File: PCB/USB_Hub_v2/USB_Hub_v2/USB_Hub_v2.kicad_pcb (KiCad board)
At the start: 2 copper layers, 63.2 x 106.8 mm, 54 parts, among them J1 USB_A, J2 USB_A, J3 USB_A, J4 USB_A, J5 USB_A, J6 USB_A, SW1 SW_Push_DPDT, U1 FE1.1s, U2 TS3USB30EDGSR, U3 TPS2116DRL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

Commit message: Update PCB layout: stackup, nets and footprints
Add recent PCB backup archives and apply extensive KiCad PCB updates: define board stackup and layer types (B.Cu -> power), rename/reorder nets, and replace/update multiple footprints and component properties (resistors, capacitors, pads, models, references and values). Adjust pad positions, sizes and net assignments, update 3D model links and footprint metadata to match revised layout. These changes appear to be automated footprint/housekeeping edits and netlist/stack adjustments to prepare the board for updated fabrication/assembly.
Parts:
- added C14: 22p, Capacitor_SMD:C_0805_2012Metric_Pad1.18x1.45mm_HandSolder, F.Cu at (75.7, 104.8)
- added C15: 22p, Capacitor_SMD:C_0805_2012Metric_Pad1.18x1.45mm_HandSolder, F.Cu at (71.5, 104.8)
- added C16: 2n2, Capacitor_SMD:C_0805_2012Metric_Pad1.18x1.45mm_HandSolder, F.Cu at (30.6, 109.2)
- added C17: 2n2, Capacitor_SMD:C_0805_2012Metric_Pad1.18x1.45mm_HandSolder, F.Cu at (29.6, 90.8)
- added C18: 2n2, Capacitor_SMD:C_0805_2012Metric_Pad1.18x1.45mm_HandSolder, F.Cu at (30.1, 76.5)
- added C19: 2n2, Capacitor_SMD:C_0805_2012Metric_Pad1.18x1.45mm_HandSolder, F.Cu at (30.3, 56.9)
- added C20: 2n2, Capacitor_SMD:C_0805_2012Metric_Pad1.18x1.45mm_HandSolder, F.Cu at (109.1, 126.6)
- added C21: 2n2, Capacitor_SMD:C_0805_2012Metric_Pad1.18x1.45mm_HandSolder, F.Cu at (36.0, 126.2)
- added C22: 100n, Capacitor_SMD:C_0805_2012Metric_Pad1.18x1.45mm_HandSolder, F.Cu at (98.5, 108.1)
- added C23: 10u, Capacitor_SMD:C_0805_2012Metric_Pad1.18x1.45mm_HandSolder, F.Cu at (80.7, 106.3)
- added C24: 100n, Capacitor_SMD:C_0805_2012Metric_Pad1.18x1.45mm_HandSolder, F.Cu at (99.1, 99.5)
- added C25: 10u, Capacitor_SMD:C_0805_2012Metric_Pad1.18x1.45mm_HandSolder, F.Cu at (99.1, 102.6)
- added C26: 4u7, Capacitor_SMD:C_0805_2012Metric_Pad1.18x1.45mm_HandSolder, F.Cu at (59.5, 86.2)
- added C27: 100n, Capacitor_SMD:C_0805_2012Metric_Pad1.18x1.45mm_HandSolder, F.Cu at (57.4, 86.2)
- added C28: 4u7, Capacitor_SMD:C_0805_2012Metric_Pad1.18x1.45mm_HandSolder, F.Cu at (59.2, 103.5)
- added C29: 100n, Capacitor_SMD:C_0805_2012Metric_Pad1.18x1.45mm_HandSolder, F.Cu at (57.2, 103.5)
- added C30: 4u7, Capacitor_SMD:C_0805_2012Metric_Pad1.18x1.45mm_HandSolder, F.Cu at (59.7, 120.8)
- added C31: 100n, Capacitor_SMD:C_0805_2012Metric_Pad1.18x1.45mm_HandSolder, F.Cu at (57.7, 120.8)
- added C32: 4u7, Capacitor_SMD:C_0805_2012Metric_Pad1.18x1.45mm_HandSolder, F.Cu at (86.1, 129.6)
- added C33: 100n, Capacitor_SMD:C_0805_2012Metric_Pad1.18x1.45mm_HandSolder, F.Cu at (88.1, 129.6)
- added C34: 100n, Capacitor_SMD:C_0805_2012Metric_Pad1.18x1.45mm_HandSolder, F.Cu at (83.5, 60.2)
- added R10: 1M, Resistor_SMD:R_0603_1608Metric_Pad0.98x0.95mm_HandSolder, F.Cu at (29.7, 88.2)
- added R11: 1M, Resistor_SMD:R_0603_1608Metric_Pad0.98x0.95mm_HandSolder, F.Cu at (30.1, 73.8)
- added R12: 1M, Resistor_SMD:R_0603_1608Metric_Pad0.98x0.95mm_HandSolder, F.Cu at (30.5, 54.1)
- added R13: 1M, Resistor_SMD:R_0603_1608Metric_Pad0.98x0.95mm_HandSolder, F.Cu at (109.0, 123.5)
- added R14: 1M, Resistor_SMD:R_0603_1608Metric_Pad0.98x0.95mm_HandSolder, F.Cu at (35.8, 123.1)
- added R9: 1M, Resistor_SMD:R_0603_1608Metric_Pad0.98x0.95mm_HandSolder, F.Cu at (30.8, 106.3)
- C1, C13: value 10uF -> 10u
- C10, C11, C12, C8: value 1-4.7uF -> 100n
- C2: value 10uF -> 100n
- C3: value 0.1uF -> 100n
- C4, C5, C6: value 1uF -> 1u
- C7, C9: value 1-4.7uF -> 4u7
- Y1: value Crystal -> 12MHz
- moved C10 69.9 mm to (61.0, 64.7)
- moved C9 56.2 mm to (63.0, 64.7), turned to -90 degrees
- moved C8 56.0 mm to (61.0, 47.5), turned to -90 degrees
- moved C7 38.9 mm to (63.0, 47.5), turned to -90 degrees
- moved C11 17.5 mm to (73.1, 56.5), turned to -90 degrees
- moved C12 14.2 mm to (72.7, 64.6), turned to 180 degrees
- moved D7 4.44 mm to (57.8, 64.4)
- moved D6 4.34 mm to (57.9, 47.1)
- moved Y1 1.60 mm to (73.7, 100.0)
- moved C2 1.26 mm to (78.7, 106.3), turned to -90 degrees
- moved U6 1.14 mm to (58.4, 125.3)
- moved U9 1.04 mm to (58.5, 69.4)
- moved U5 1.01 mm to (58.5, 108.0)
- moved U4 0.94 mm to (58.6, 90.7)
- moved U8 0.75 mm to (58.5, 52.1)
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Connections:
- net /DM3 renamed /D3-
- net /DM4 renamed /D4-
- net /DMU renamed /DSW-
- net /DP3 renamed /D3+
- net /DP4 renamed /D4+
- net /DPU renamed /DSW+
- net Net-(J1-D+) renamed /DIN4+
- net Net-(J1-D-) renamed /DIN4-
- net Net-(J2-D+) renamed /DIN3+
- net Net-(J2-D-) renamed /DIN3-
- net Net-(J3-D+) renamed /DIN2+
- net Net-(J3-D-) renamed /DIN2-
- net Net-(J4-D+) renamed /DIN1+
- net Net-(J4-D-) renamed /DIN1-
- net Net-(J5-D+) renamed /DINPC1+
- net Net-(J5-D-) renamed /DINPC1-
- net Net-(J6-D+) renamed /DINPC2+
- net Net-(J6-D-) renamed /DINPC2-
- net Net-(U1-VD18) renamed /1V8
- C10 pad 1: /5V -> GND
- C10 pad 2: GND -> /5V_2
- C11 pad 1: /5V_1 -> /5V
- C12 pad 1: /5V_2 -> /5V_1
- C13 pad 1: /5V -> GND
- C13 pad 2: GND -> /5V
- C7 pad 1: /5V -> GND
- C7 pad 2: GND -> /5V_1
- C8 pad 1: /5V -> GND
- C8 pad 2: GND -> /5V_1
- C9 pad 1: /5V -> GND
- C9 pad 2: GND -> /5V_2
- J1 pad 5: GND -> Net-(J1-Shield)
- J2 pad 5: GND -> Net-(J2-Shield)
- J3 pad 5: GND -> Net-(J3-Shield)
- J4 pad 5: GND -> Net-(J4-Shield)
- J5 pad 5: GND -> Net-(J5-Shield)
- J6 pad 5: GND -> Net-(J6-Shield)
- U1 pad 10: /DM1 -> /D1-
- U1 pad 11: /DP1 -> /D1+
- U1 pad 8: /DM2 -> /D2-
- U1 pad 9: /DP2 -> /D2+
- U2 pad 2: /D1+ -> /DPC1+
- U2 pad 3: /D2+ -> /DPC2+
- U2 pad 7: /D2- -> /DPC2-
- U2 pad 8: /D1- -> /DPC1-
- U6 pad 1: /DP2 -> /D2+
- U6 pad 3: /DM2 -> /D2-
- U7 pad 1: /DP1 -> /D1+
- U7 pad 3: /DM1 -> /D1-
- U8 pad 1: /D1+ -> /DPC1+
- U8 pad 3: /D1- -> /DPC1-
- U9 pad 1: /D2+ -> /DPC2+
- U9 pad 3: /D2- -> /DPC2-
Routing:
- net GND: track 101.5 -> 64.6 mm, vias 9 -> 17
- net /DM1: track 35.2 -> 0.00 mm
- net /DP1: track 31.3 -> 0.00 mm
- net /D4-: track 25.8 -> 0.00 mm
- net /D4+: track 25.1 -> 0.00 mm
- net /DP2: track 22.1 -> 0.00 mm
- net /DPC1-: track 0.00 -> 21.5 mm, vias 0 -> 2
- net /DM2: track 20.9 -> 0.00 mm
- net /DPC1+: track 0.00 -> 18.8 mm, vias 0 -> 2
- net /D2+: track 3.92 -> 20.6 mm
- net /5V: track 293.0 -> 280.3 mm, vias 4 -> 6
- net /D3-: track 11.6 -> 0.00 mm
- net /D3+: track 11.1 -> 0.00 mm
- net /DPC2-: track 0.00 -> 9.35 mm
- net /D2-: track 11.3 -> 20.6 mm
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
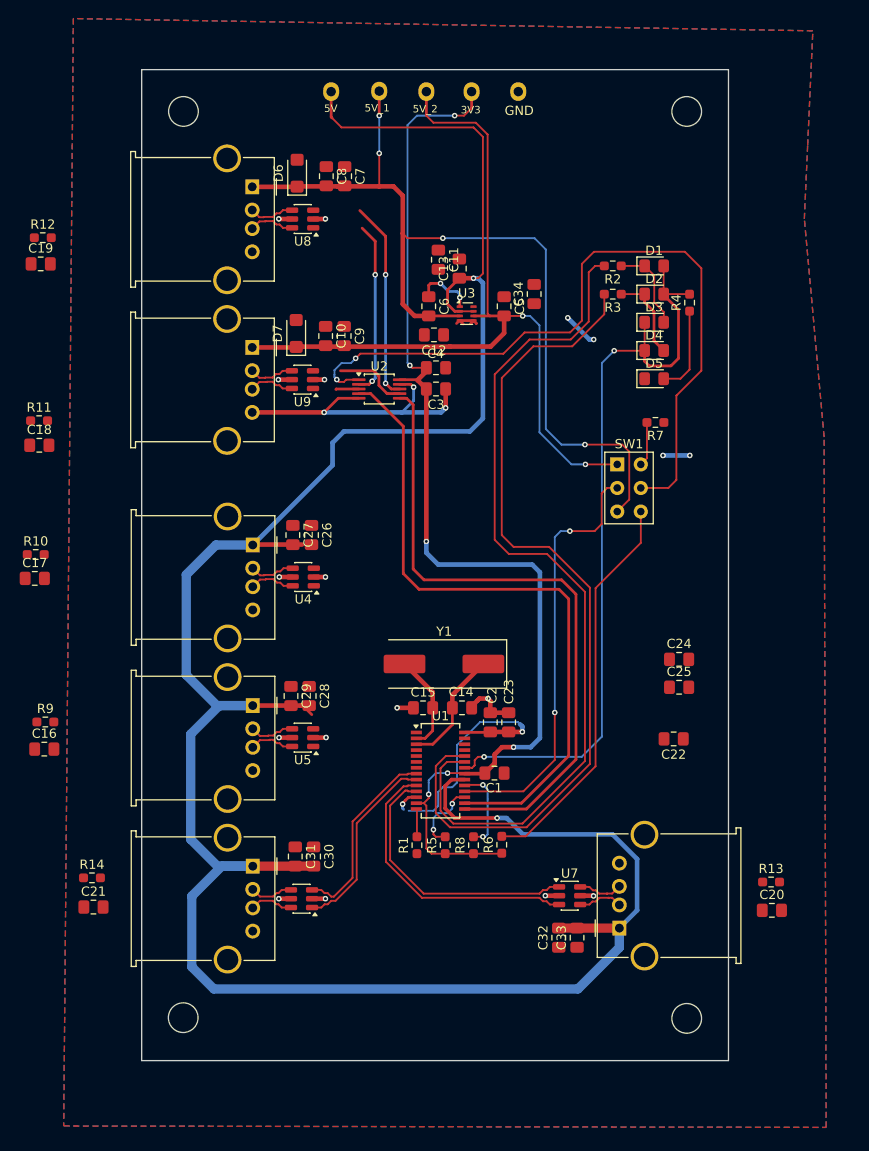
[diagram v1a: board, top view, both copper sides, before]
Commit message: Adjust KiCad footprints and add backups
Rotate/reposition multiple SMD footprints, update pad rotations, fp_line/fp_text orientations and UUIDs in USB_Hub_v2.kicad_pcb (and related project files). Also update USB_Hub_v2.kicad_pro/.kicad_sch metadata to match footprint changes. Add five timestamped backup ZIPs under USB_Hub_v2-backups. These edits correct component orientations/placements and record backups.
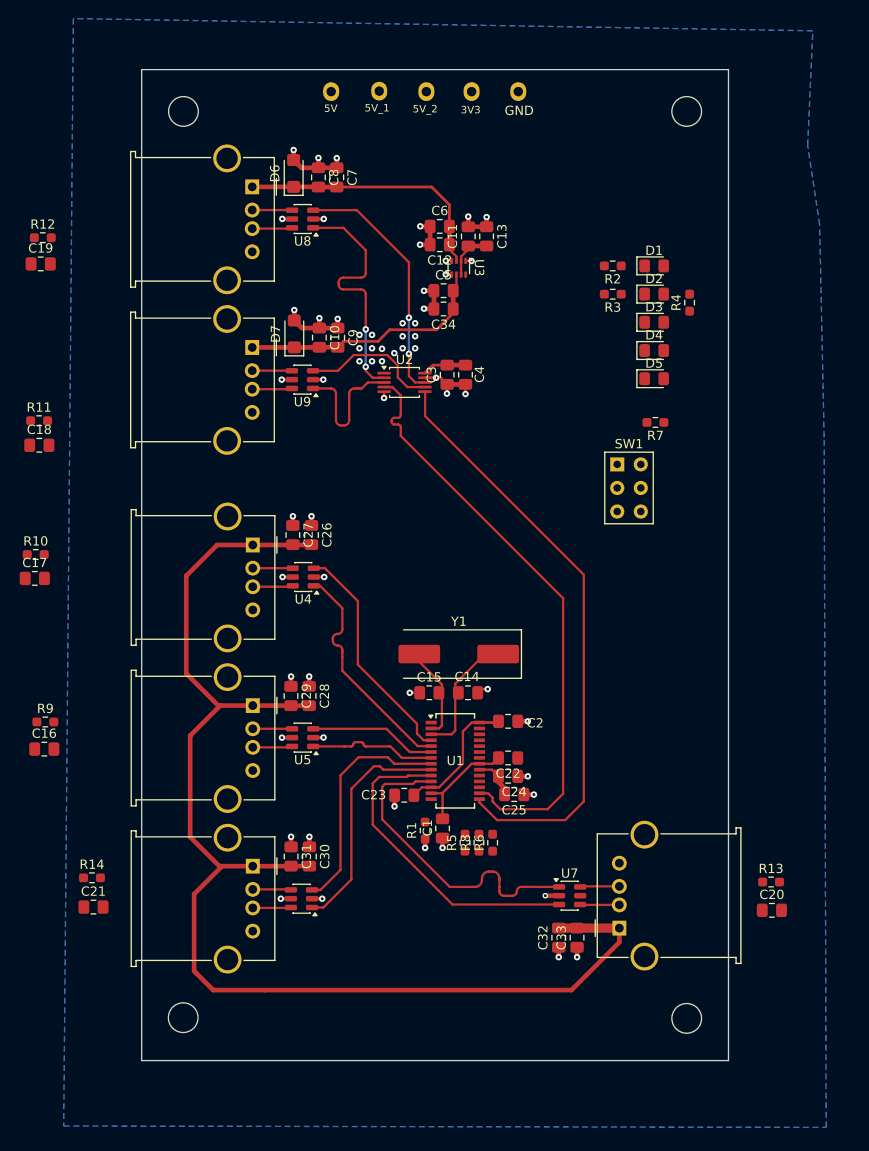
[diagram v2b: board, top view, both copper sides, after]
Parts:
- moved C24 22.3 mm to (80.6, 112.2), turned to 180 degrees
- moved C25 21.2 mm to (81.3, 114.1), turned to 180 degrees
- moved C22 18.0 mm to (80.6, 110.2)
- moved C23 13.7 mm to (69.5, 114.2), turned to 0 degrees
- moved C34 9.89 mm to (73.7, 61.8), turned to 180 degrees
- moved C12 9.74 mm to (73.3, 54.9)
- moved C6 8.69 mm to (73.3, 52.9), turned to 0 degrees
- moved C1 8.18 mm to (73.6, 117.8), turned to 90 degrees
- moved C5 6.74 mm to (73.7, 59.8), turned to 0 degrees
- moved U3 5.02 mm to (75.3, 57.3), turned to -90 degrees
- moved C13 4.55 mm to (78.3, 54.0), turned to -90 degrees
- moved C11 4.09 mm to (76.3, 54.0), turned to 90 degrees
- moved C4 3.27 mm to (76.0, 68.9), turned to 90 degrees
- moved U2 2.81 mm to (69.5, 69.7)
- moved R5 2.15 mm to (76.0, 119.3)
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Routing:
- net /5V: track 280.3 -> 153.1 mm, vias 6 -> 3
- net /3.3V: track 124.0 -> 16.3 mm, vias 6 -> 0
- net /LED1: track 94.3 -> 0.00 mm
- net /LED2: track 92.6 -> 0.00 mm
- net /LED_DRV: track 83.8 -> 0.00 mm, vias 2 -> 0
- net /S_TS3USB: track 81.0 -> 0.00 mm, vias 2 -> 0
- net /5V_1: track 99.3 -> 29.5 mm, vias 5 -> 1
- net /5V_2: track 90.1 -> 28.6 mm, vias 3 -> 1
- net /VBUS: track 46.0 -> 0.00 mm, vias 2 -> 0
- net Net-(R6-Pad2): track 42.7 -> 0.00 mm
- net /D4-: track 0.00 -> 25.0 mm
- net /D4+: track 0.00 -> 24.9 mm
- net /1V8: track 28.9 -> 14.3 mm, vias 2 -> 0
- net /D3-: track 0.00 -> 13.7 mm
- net /D3+: track 0.00 -> 13.7 mm
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- removed copper zone on F.Cu, net GND

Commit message: Update KiCad PCB footprints, nets & backups
Enable dielectric constraints and introduce Net-(U2-S) (net 58); correct several pad/net assignments to use Net-(U2-S) instead of the old net, and update many footprint positions, rotations, silk/fab text orientations and UUIDs. Add a new C35 0805 capacitor footprint and other resized/rotated SMD footprints (resistors, caps), plus layout refinements. Also remove older backup ZIPs and add new backup archives. These changes adjust component placement/orientation and net mapping to match the updated board layout.
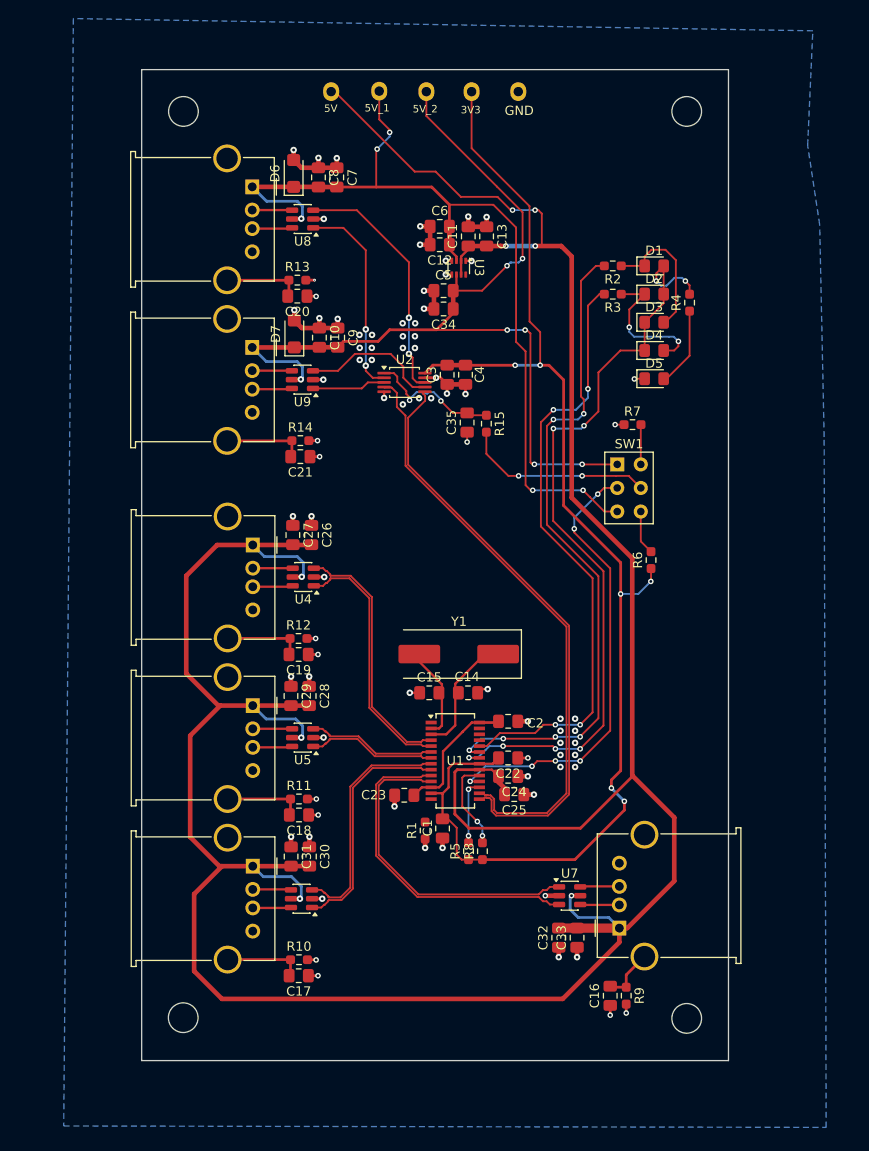
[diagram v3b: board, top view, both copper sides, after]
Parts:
- added C35: 100n, Capacitor_SMD:C_0805_2012Metric_Pad1.18x1.45mm_HandSolder, F.Cu at (76.2, 74.0)
- added R15: 1k, Resistor_SMD:R_0603_1608Metric_Pad0.98x0.95mm_HandSolder, F.Cu at (78.3, 74.2)
- moved C20 83.7 mm to (57.9, 60.4), turned to 180 degrees
- moved R13 82.6 mm to (57.9, 58.7)
- moved R9 69.2 mm to (93.4, 135.8), turned to -90 degrees
- moved C16 66.5 mm to (91.7, 135.8), turned to 90 degrees
- moved C21 53.4 mm to (58.2, 77.7), turned to 180 degrees
- moved R14 52.2 mm to (58.2, 76.0)
- moved R10 52.1 mm to (58.1, 131.9)
- moved C17 51.4 mm to (58.1, 133.7), turned to 180 degrees
- moved R12 51.2 mm to (58.0, 97.3)
- moved C19 50.5 mm to (58.1, 99.0), turned to 180 degrees
- moved R11 49.5 mm to (58.1, 114.6)
- moved C18 48.7 mm to (58.1, 116.3), turned to 180 degrees
- moved R6 34.9 mm to (96.0, 88.8)
- moved R7 2.48 mm to (94.0, 74.2), turned to 0 degrees
- moved R5 0.99 mm to (76.4, 120.2)
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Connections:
- U2 pad 1: /S_TS3USB -> Net-(U2-S)
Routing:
- net /5V: track 153.1 -> 335.7 mm, vias 3 -> 8
- net /3.3V: track 16.3 -> 141.8 mm, vias 0 -> 6
- net /LED_DRV: track 0.00 -> 84.7 mm, vias 0 -> 8
- net /LED1: track 0.00 -> 72.5 mm, vias 0 -> 6
- net /5V_2: track 28.6 -> 101.0 mm, vias 1 -> 7
- net /5V_1: track 29.5 -> 95.9 mm, vias 1 -> 5
- net /LED2: track 0.00 -> 65.6 mm, vias 0 -> 4
- net /VBUS: track 0.00 -> 48.9 mm, vias 0 -> 6
- net /S_TS3USB: track 0.00 -> 20.5 mm, vias 0 -> 2
- net GND: track 62.4 -> 78.7 mm, vias 56 -> 82
- net Net-(D2-K): track 0.00 -> 15.3 mm, vias 0 -> 2
- net Net-(D1-K): track 0.00 -> 15.0 mm
- net Net-(U2-S): track 0.00 -> 14.6 mm, vias 0 -> 2
- net Net-(J2-Shield): track 0.00 -> 12.6 mm
- net Net-(U1-BUSJ): track 0.00 -> 9.86 mm, vias 0 -> 2
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
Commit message: Update PCB layout: reroute nets and add backups
Add multiple USB_Hub_v2 backup zip snapshots and update KiCad project files. USB_Hub_v2.kicad_pcb: swap DPC1/DPC2 net assignments, hide C9 silkscreen reference, and apply extensive track/via repositioning and rerouting (many segment coordinate/width and via size/position adjustments and UUID updates). Also modify the project and schematic files (.kicad_pro, .kicad_sch) to reflect these PCB changes.
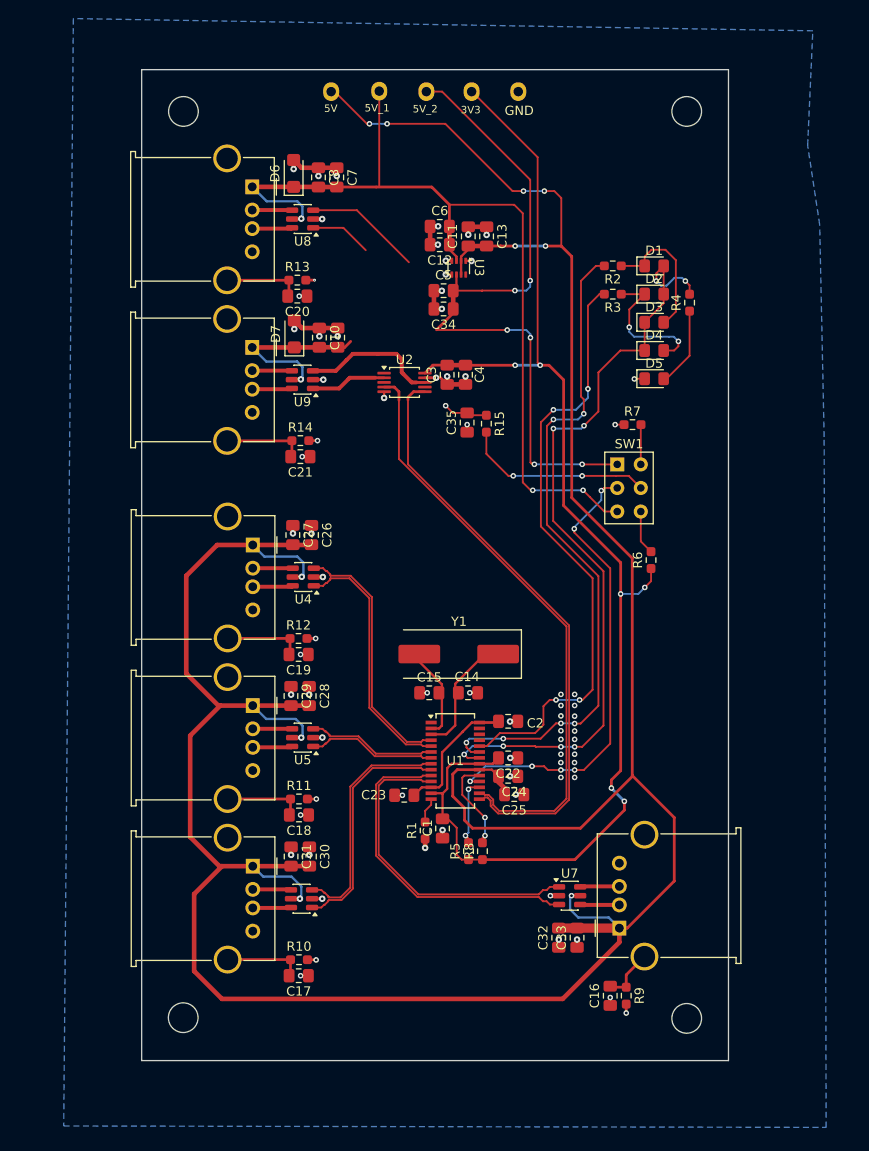
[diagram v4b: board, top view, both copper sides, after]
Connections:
- U2 pad 2: /DPC1+ -> /DPC2+
- U2 pad 3: /DPC2+ -> /DPC1+
- U2 pad 7: /DPC2- -> /DPC1-
- U2 pad 8: /DPC1- -> /DPC2-
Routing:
- net /DPC1+: track 21.9 -> 6.66 mm, vias 2 -> 0
- net /DPC1-: track 26.8 -> 12.6 mm, vias 2 -> 0
- net Net-(U2-S): track 14.6 -> 4.81 mm, vias 2 -> 1
- net GND: track 78.7 -> 70.0 mm, vias 82 -> 73
- net /5V_2: track 101.0 -> 95.1 mm
- net /5V: track 335.7 -> 338.8 mm, vias 8 -> 10
- net Net-(U1-REXT): track 0.00 -> 2.74 mm
- net /VBUS: track 48.9 -> 50.0 mm
- net /LED_DRV: track 84.7 -> 85.6 mm
- net /5V_1: track 95.9 -> 96.2 mm, vias 5 -> 3
